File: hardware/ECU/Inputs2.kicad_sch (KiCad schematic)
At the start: 9 parts, among them Q2 Q_DUAL_NMOS_S1G1D2S2G2D1, U14 LMV324LIDT

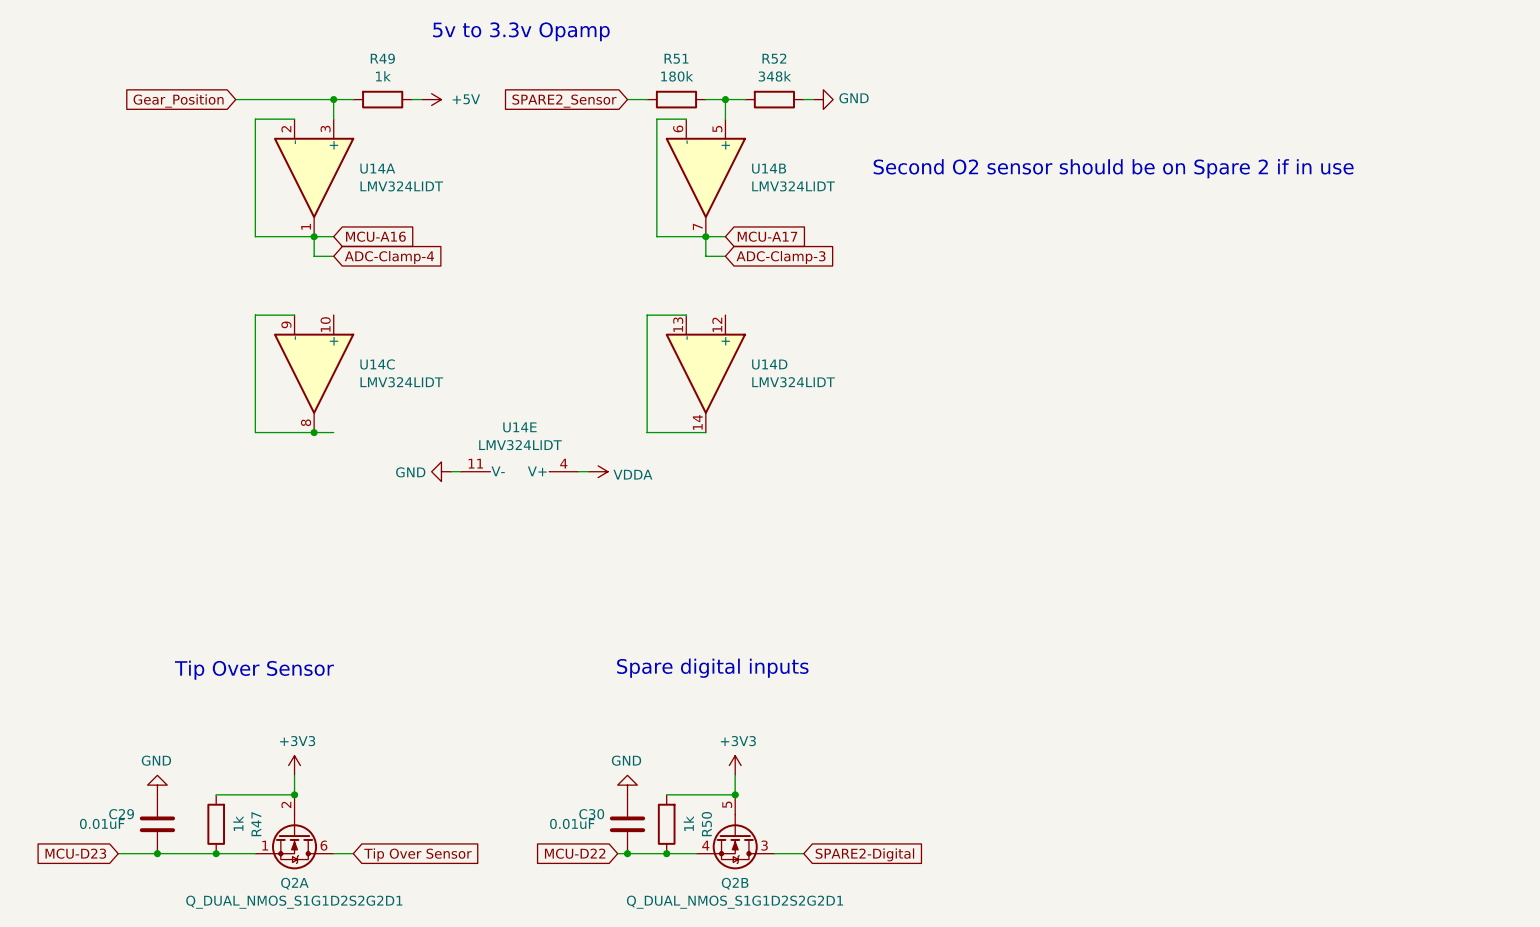
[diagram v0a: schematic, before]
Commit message: Replace speeduino submodule with HasiKe fork, fix teensy.pretty path
- Switch speeduino from speeduino/speeduino to HasiKe/speeduino
- Fix teensy.pretty submodule path case mismatch (Hardware -> hardware)
- Add ISL9V5036P3-F085 component library
- Various ECU schematic updates
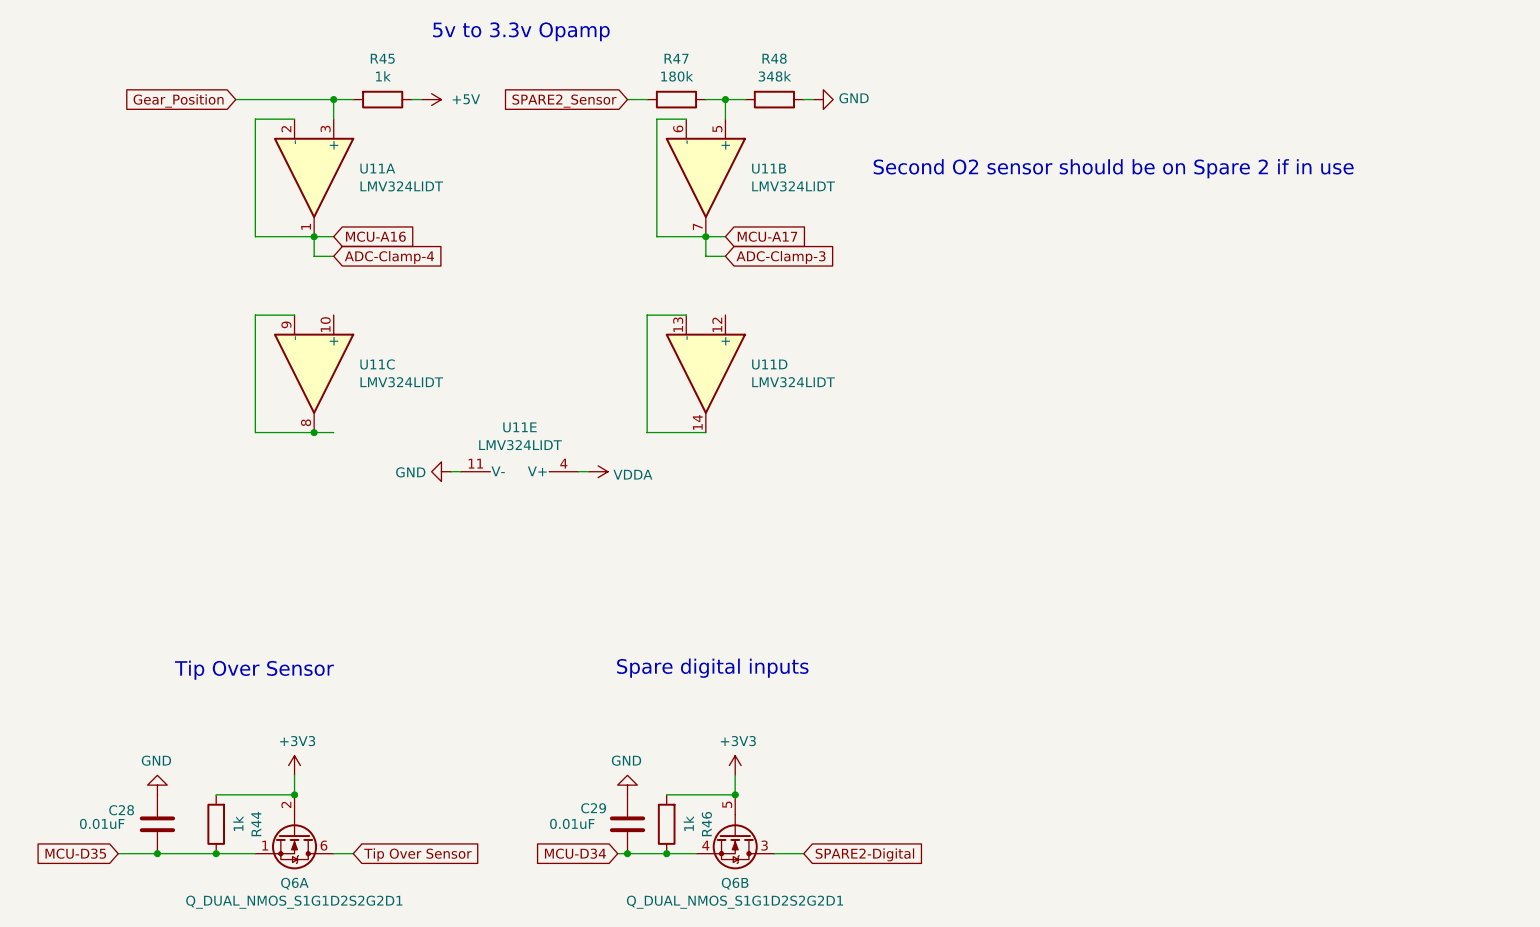
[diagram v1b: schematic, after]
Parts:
- renumbered C29 to C28, C30 to C29, Q2 to Q6, R47 to R44, R49 to R45, R50 to R46, R51 to R47, R52 to R48, U14 to U11
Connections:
- net MCU-D22 renamed MCU-D34
- net MCU-D23 renamed MCU-D35
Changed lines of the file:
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@@
 		)
 	)
-	(global_label "MCU-D22"
+	(global_label "MCU-D34"
 		(shape input)
 		(at 154.94 147.32 180)
@@
 		)
 		(property "Intersheetrefs" "${INTERSHEET_REFS}"
-			(at 143.3751 147.32 0)
+			(at 142.6415 147.32 0)
 			(effects
 				(font
@@
 		)
 	)
-	(global_label "MCU-D23"
+	(global_label "MCU-D35"
 		(shape input)
 		(at 90.17 147.32 180)
@@
 		)
 		(property "Intersheetrefs" "${INTERSHEET_REFS}"
-			(at 78.6051 147.32 0)
+			(at 77.8715 147.32 0)
 			(effects
 				(font
@@
 		(on_board yes)
 		(dnp no)
-		(property "Reference" "R52"
+		(property "Reference" "R48"
 			(at 175.26 44.2722 90)
 			(effects
@@
 			(project "ECU"
 				(path "/aaebd8f9-fdac-426b-87c0-a208167b6035/208a416e-a5c2-4c6c-835c-57e49c0491be"
-					(reference "R52")
+					(reference "R48")
 					(unit 1)
 				)
@@
 		(on_board yes)
 		(dnp no)
-		(property "Reference" "C30"
-			(at 149.86 142.24 0)
+		(property "Reference" "C29"
+			(at 150.114 141.478 0)
 			(effects
 				(font
@@
 			(project "ECU"
 				(path "/aaebd8f9-fdac-426b-87c0-a208167b6035/208a416e-a5c2-4c6c-835c-57e49c0491be"
-					(reference "C30")
+					(reference "C29")
 					(unit 1)
 				)
@@
 		(on_board yes)
 		(dnp no)
-		(property "Reference" "#PWR078"
+		(property "Reference" "#PWR079"
 			(at 113.03 140.97 0)
 			(effects
@@
 			(project "ECU"
 				(path "/aaebd8f9-fdac-426b-87c0-a208167b6035/208a416e-a5c2-4c6c-835c-57e49c0491be"
-					(reference "#PWR078")
+					(reference "#PWR079")
 					(unit 1)
 				)
@@
 		(on_board yes)
 		(dnp no)
-		(property "Reference" "Q2"
+		(property "Reference" "Q6"
 			(at 113.03 151.1554 90)
 			(effects
@@
 			(project "ECU"
 				(path "/aaebd8f9-fdac-426b-87c0-a208167b6035/208a416e-a5c2-4c6c-835c-57e49c0491be"
-					(reference "Q2")
+					(reference "Q6")
 					(unit 1)
 				)
@@
 		(on_board yes)
 		(dnp no)
-		(property "Reference" "R50"
+		(property "Reference" "R46"
 			(at 166.5478 143.51 90)
 			(effects
@@
 			(project "ECU"
 				(path "/aaebd8f9-fdac-426b-87c0-a208167b6035/208a416e-a5c2-4c6c-835c-57e49c0491be"
-					(reference "R50")
+					(reference "R46")
 					(unit 1)
 				)
@@
 		(dnp no)
 		(fields_autoplaced yes)
-		(property "Reference" "#PWR08"
+		(property "Reference" "#PWR080"
 			(at 125.73 49.53 0)
 			(effects
@@
 			(project ""
 				(path "/aaebd8f9-fdac-426b-87c0-a208167b6035/208a416e-a5c2-4c6c-835c-57e49c0491be"
-					(reference "#PWR08")
+					(reference "#PWR080")
 					(unit 1)
 				)
@@
 		(on_board yes)
 		(dnp no)
-		(property "Reference" "#PWR082"
+		(property "Reference" "#PWR083"
 			(at 156.21 133.35 0)
 			(effects
@@
 			(project "ECU"
 				(path "/aaebd8f9-fdac-426b-87c0-a208167b6035/208a416e-a5c2-4c6c-835c-57e49c0491be"
-					(reference "#PWR082")
+					(reference "#PWR083")
 					(unit 1)
 				)
@@
 		(on_board yes)
 		(dnp no)
-		(property "Reference" "U14"
+		(property "Reference" "U11"
 			(at 142.24 92.075 90)
 			(effects
@@
 			(project "ECU"
 				(path "/aaebd8f9-fdac-426b-87c0-a208167b6035/208a416e-a5c2-4c6c-835c-57e49c0491be"
-					(reference "U14")
+					(reference "U11")
 					(unit 5)
 				)
@@
 		(on_board yes)
 		(dnp no)
-		(property "Reference" "R47"
+		(property "Reference" "R44"
 			(at 108.1278 143.51 90)
 			(effects
@@
 			(project "ECU"
 				(path "/aaebd8f9-fdac-426b-87c0-a208167b6035/208a416e-a5c2-4c6c-835c-57e49c0491be"
-					(reference "R47")
+					(reference "R44")
 					(unit 1)
 				)
@@
 		(on_board yes)
 		(dnp no)
-		(property "Reference" "R49"
+		(property "Reference" "R45"
 			(at 124.46 44.2722 90)
 			(effects
@@
 			(project "ECU"
 				(path "/aaebd8f9-fdac-426b-87c0-a208167b6035/208a416e-a5c2-4c6c-835c-57e49c0491be"
-					(reference "R49")
+					(reference "R45")
 					(unit 1)
 				)
@@
 		(on_board yes)
 		(dnp no)
-		(property "Reference" "#PWR084"
+		(property "Reference" "#PWR085"
 			(at 186.69 49.53 0)
 			(effects
@@
 			(project "ECU"
 				(path "/aaebd8f9-fdac-426b-87c0-a208167b6035/208a416e-a5c2-4c6c-835c-57e49c0491be"
-					(reference "#PWR084")
+					(reference "#PWR085")
 					(unit 1)
 				)
@@
 		(on_board yes)
 		(dnp no)
-		(property "Reference" "#PWR081"
+		(property "Reference" "#PWR082"
 			(at 147.32 97.79 0)
 			(effects
@@
 			(project "ECU"
 				(path "/aaebd8f9-fdac-426b-87c0-a208167b6035/208a416e-a5c2-4c6c-835c-57e49c0491be"
-					(reference "#PWR081")
+					(reference "#PWR082")
 					(unit 1)
 				)
@@
 		(on_board yes)
 		(dnp no)
-		(property "Reference" "#PWR080"
+		(property "Reference" "#PWR081"
 			(at 127 97.79 0)
 			(effects
@@
 			(project "ECU"
 				(path "/aaebd8f9-fdac-426b-87c0-a208167b6035/208a416e-a5c2-4c6c-835c-57e49c0491be"
-					(reference "#PWR080")
+					(reference "#PWR081")
 					(unit 1)
 				)
@@
 		(on_board yes)
 		(dnp no)
-		(property "Reference" "R51"
+		(property "Reference" "R47"
 			(at 162.56 44.2722 90)
 			(effects
@@
 			(project "ECU"
 				(path "/aaebd8f9-fdac-426b-87c0-a208167b6035/208a416e-a5c2-4c6c-835c-57e49c0491be"
-					(reference "R51")
+					(reference "R47")
 					(unit 1)
 				)
@@
 		(on_board yes)
 		(dnp no)
-		(property "Reference" "C29"
-			(at 88.9 142.24 0)
+		(property "Reference" "C28"
+			(at 88.9 141.732 0)
 			(effects
 				(font
@@
 			(project "ECU"
 				(path "/aaebd8f9-fdac-426b-87c0-a208167b6035/208a416e-a5c2-4c6c-835c-57e49c0491be"
-					(reference "C29")
+					(reference "C28")
 					(unit 1)
 				)
@@
 		(on_board yes)
 		(dnp no)
-		(property "Reference" "Q2"
+		(property "Reference" "Q6"
 			(at 170.18 151.1554 90)
 			(effects
@@
 			(project "ECU"
 				(path "/aaebd8f9-fdac-426b-87c0-a208167b6035/208a416e-a5c2-4c6c-835c-57e49c0491be"
-					(reference "Q2")
+					(reference "Q6")
 					(unit 2)
 				)
@@
 		(on_board yes)
 		(dnp no)
-		(property "Reference" "U14"
+		(property "Reference" "U11"
 			(at 172.212 58.5216 90)
 			(effects
@@
 			(project "ECU"
 				(path "/aaebd8f9-fdac-426b-87c0-a208167b6035/208a416e-a5c2-4c6c-835c-57e49c0491be"
-					(reference "U14")
+					(reference "U11")
 					(unit 2)
 				)
@@
 		(on_board yes)
 		(dnp no)
-		(property "Reference" "U14"
+		(property "Reference" "U11"
 			(at 121.412 83.9216 90)
 			(effects
@@
 			(project "ECU"
 				(path "/aaebd8f9-fdac-426b-87c0-a208167b6035/208a416e-a5c2-4c6c-835c-57e49c0491be"
-					(reference "U14")
+					(reference "U11")
 					(unit 3)
 				)
@@
 		(on_board yes)
 		(dnp no)
-		(property "Reference" "U14"
+		(property "Reference" "U11"
 			(at 121.412 58.5216 90)
 			(effects
@@
 			(project "ECU"
 				(path "/aaebd8f9-fdac-426b-87c0-a208167b6035/208a416e-a5c2-4c6c-835c-57e49c0491be"
-					(reference "U14")
+					(reference "U11")
 					(unit 1)
 				)
@@
 		(on_board yes)
 		(dnp no)
-		(property "Reference" "#PWR083"
+		(property "Reference" "#PWR084"
 			(at 170.18 140.97 0)
 			(effects
@@
 			(project "ECU"
 				(path "/aaebd8f9-fdac-426b-87c0-a208167b6035/208a416e-a5c2-4c6c-835c-57e49c0491be"
-					(reference "#PWR083")
+					(reference "#PWR084")
 					(unit 1)
 				)
@@
 		(on_board yes)
 		(dnp no)
-		(property "Reference" "#PWR077"
+		(property "Reference" "#PWR078"
 			(at 95.25 133.35 0)
 			(effects
@@
 			(project "ECU"
 				(path "/aaebd8f9-fdac-426b-87c0-a208167b6035/208a416e-a5c2-4c6c-835c-57e49c0491be"
-					(reference "#PWR077")
+					(reference "#PWR078")
 					(unit 1)
 				)
@@
 		(on_board yes)
 		(dnp no)
-		(property "Reference" "U14"
+		(property "Reference" "U11"
 			(at 172.212 83.9216 90)
 			(effects
@@
 			(project "ECU"
 				(path "/aaebd8f9-fdac-426b-87c0-a208167b6035/208a416e-a5c2-4c6c-835c-57e49c0491be"
-					(reference "U14")
+					(reference "U11")
 					(unit 4)
 				)
